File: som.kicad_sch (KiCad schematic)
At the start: 0 parts

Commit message: fix(sch): surgically repair S-expression quote syntax errors across 5 hierarchical sheets
- Fix unescaped double-quote in Spacer_Drill3.7mm_H4mm description on interfaces.kicad_sch line 1459
- Remove backslash-escaped quotes in symbol definitions and lib_id references across display, id-serial, som, and usb-debug sheets (332 lines)
- Restore clean hierarchical schematic loading in KiCad 10 GUI and CLI
- Verified with kicad-cli sch export netlist (full 300 components / 437 nets recovered) and sch erc
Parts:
- added BAT1: Battery_Holder_MS621FE-FL11E, jetson-footprints:MS621FE-FL11E, symbol jetson-symbols:Battery_Holder_MS621FE-FL11E
- added BOOT1, PWR1, USER1: LED_G_0603_LG_L29K-G2J1-24-Z, jetson-footprints:LED_0603_1608Metric_G, symbol jetson-symbols:LED_G_0603_LG_L29K-G2J1-24-Z
- added C10, C11: C_Pol_330u_6.3V_KEMET-T520-B, jetson-footprints:C_Pol_EIA-B, symbol jetson-symbols:C_Pol_330u_6.3V_KEMET-T520-B
- added FB2: FB_10Z_10A_WE-MPSB_1206, jetson-footprints:FB_1206_3216Metric, symbol jetson-symbols:FB_10Z_10A_WE-MPSB_1206
- added J10: Conn_FFC_Molex_5051101097, jetson-footprints:Conn_FFC_Molex_5051101097, symbol jetson-symbols:Conn_FFC_Molex_5051101097
- added J15: Bus_DDR4_SODIMM_CUSTOM_Jetson-Nano-H9.2mm-socket, jetson-footprints:TE_2309413, symbol jetson-symbols:Bus_DDR4_SODIMM_CUSTOM_Jetson-Nano-H9.2mm-socket
- added M2: Jetson-Nano, jetson-footprints:Module_Jetson-Nano, symbol jetson-symbols:Jetson-Nano
- added R111, R14, R97: R_470R_0402, jetson-footprints:R_0402_1005Metric, symbol jetson-symbols:R_470R_0402
- added R112, R113, R139: R_100k_0402, jetson-footprints:R_0402_1005Metric, symbol jetson-symbols:R_100k_0402
- added REC1, RST1, USR1: SW_TL3340AF160QG_SMD, jetson-footprints:SW_TL3340AF160QG_SMD, symbol jetson-symbols:SW_TL3340AF160QG_SMD
- added SP1, SP2, SP3, SP4, SP5, SP6: Spacer_Drill3.7mm_H6mm_9774060151R, jetson-footprints:Spacer_Drill3.7mm_H6mm_9774060151R, symbol jetson-symbols:Spacer_Drill3.7mm_H6mm_9774060151R
- added T2, T4, T5: BSS138PW, jetson-footprints:SC70-3, symbol jetson-symbols:BSS138PW
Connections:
- new net: T5.3 (D), USER1.1 (C)
- new net: R111.2, USER1.2 (A)
- new net: PWR1.1 (C), T4.3 (D)
- new net: PWR1.2 (A), R97.2
- new net: BOOT1.1 (C), T2.3 (D)
- new net: BOOT1.2 (A), R14.2
- new net #PWR_BUTTON: J15.240 (SLEEP/~{WAKE})
- new net #RECOVERY: J15.214 (~{FORCE_RECOVERY}), REC1.2
- new net #RESET: J15.239 (~{SYS_RESET}), R139.1, RST1.2, T2.1 (G)
- new net #SHUTDOWN_REQ: J15.233 (~{SHUTDOWN_REQ})
- new net 1V8_SYS: R112.1
- new net 3V3_SYS: J10.1
- new net 5V0_SYS: FB2.1, R111.1, R14.1, R97.1
- new net CAN_RXD: J15.143 ((CAN_RX)RSVD)
- new net CAN_TXD: J15.145 ((CAN_TX)RSVD)
- new net EGND: SP4.1
- new net ENET_LED0: J15.194 (GBE_LED_ACT)
- new net ENET_LED1: J15.188 (GBE_LED_LINK)
- new net ENET_TRD0_N: J15.184 (GBE_MDI0_N)
- new net ENET_TRD0_P: J15.186 (GBE_MDI0_P)
- new net ENET_TRD1_N: J15.190 (GBE_MDI1_N)
- new net ENET_TRD1_P: J15.192 (GBE_MDI1_P)
- new net ENET_TRD2_N: J15.196 (GBE_MDI2_N)
- new net ENET_TRD2_P: J15.198 (GBE_MDI2_P)
- new net ENET_TRD3_N: J15.202 (GBE_MDI3_N)
- new net ENET_TRD3_P: J15.204 (GBE_MDI3_P)
- new net FAN_PWM: J15.230 (GPIO14)
- new net FAN_TACH: J15.208 (GPIO08)
- new net GEN0_SCL: J15.185 (I2C0_SCL)
- new net GEN0_SDA: J15.187 (I2C0_SDA)
- new net GND: BAT1.2 (-), C10.2, C11.2, J10.10, J15.1 (GND), J15.102 (GND), J15.107 (GND), J15.113 (GND), J15.119 (GND), J15.125 (GND), J15.129 (GND), J15.13 (GND), J15.132 (GND), J15.135 (GND), J15.138 (GND), J15.14 (GND), J15.141 (GND), J15.144 (GND), J15.146 (GND), J15.147 (GND), J15.152 (GND), J15.153 (GND), J15.158 (GND), J15.159 (GND), J15.164 (GND), J15.165 (GND), J15.170 (GND), J15.171 (GND), J15.176 (GND), J15.177 (GND), J15.19 (GND), J15.2 (GND), J15.20 (GND), J15.200 (GND), J15.201 (GND), J15.217 (GND), J15.231 (GND), J15.241 (GND), J15.242 (GND), J15.243 (GND), J15.244 (GND), J15.245 (GND), J15.246 (GND), J15.247 (GND), J15.248 (GND), J15.249 (GND), J15.25 (GND), J15.250 (GND), J15.26 (GND), J15.261 (MNT), J15.262 (MNT), J15.31 (GND), J15.32 (GND), J15.37 (GND), J15.38 (GND), J15.43 (GND), J15.44 (GND), J15.49 (GND), J15.50 (GND), J15.55 (GND), J15.56 (GND), J15.61 (GND), J15.62 (GND), J15.67 (GND), J15.68 (GND), J15.7 (GND), J15.73 (GND), J15.74 (GND), J15.79 (GND), J15.8 (GND), J15.80 (GND), J15.85 (GND), J15.86 (GND), R113.1, R139.2, REC1.1, REC1.3, REC1.SH, RST1.1, RST1.3, RST1.SH, SP1.1, SP2.1, SP3.1, SP5.1, SP6.1, T2.2 (S), T4.2 (S), T5.2 (S), USR1.1, USR1.3, USR1.SH
- new net I2C1_SCL: J15.189 (I2C1_SCL)
- new net I2C1_SDA: J15.191 (I2C1_SDA)
- new net I2C_MUX_RESET: J15.127 (GPIO04)
- new net OTG_USB_D_N: J15.109 (USB0_D_N)
- new net OTG_USB_D_P: J15.111 (USB0_D_P)
- new net PCIE0_CLK_N: J15.160 (PCIE0_CLK_N)
- new net PCIE0_CLK_P: J15.162 (PCIE0_CLK_P)
- new net PCIE0_RX0_N: J15.131 (PCIE0_RX0_N)
- new net PCIE0_RX0_P: J15.133 (PCIE0_RX0_P)
- new net PCIE0_RX1_N: J15.137 (PCIE0_RX1_N)
- new net PCIE0_RX1_P: J15.139 (PCIE0_RX1_P)
- new net PCIE0_RX2_N: J15.149 (PCIE0_RX2_N)
- new net PCIE0_RX2_P: J15.151 (PCIE0_RX2_P)
- new net PCIE0_RX3_N: J15.155 (PCIE0_RX3_N)
- new net PCIE0_RX3_P: J15.157 (PCIE0_RX3_P)
- new net PCIE0_TX0_N: J15.134 (PCIE0_TX0_N)
- new net PCIE0_TX0_P: J15.136 (PCIE0_TX0_P)
- new net PCIE0_TX1_N: J15.140 (PCIE0_TX1_N)
- new net PCIE0_TX1_P: J15.142 (PCIE0_TX1_P)
- new net PCIE0_TX2_N: J15.148 (PCIE0_TX2_N)
- new net PCIE0_TX2_P: J15.150 (PCIE0_TX2_P)
- new net PCIE0_TX3_N: J15.154 (PCIE0_TX3_N)
- new net PCIE0_TX3_P: J15.156 (PCIE0_TX3_P)
- new net PCIE1_CLKREQ: J10.3, J15.182 (PCIE1_CLKREQ)
- new net PCIE1_CLK_N: J10.5, J15.173 (PCIE1_CLK_N)
- new net PCIE1_CLK_P: J10.4, J15.175 (PCIE1_CLK_P)
- new net PCIE1_RST: J10.2, J15.183 (PCIE1_RST)
- new net PCIE1_RX0_N: J10.9, J15.167 (PCIE1_RX0_N)
- new net PCIE1_RX0_P: J10.8, J15.169 (PCIE1_RX0_P)
- new net PCIE1_TX0_N: J10.7, J15.172 (PCIE1_TX0_N)
- new net PCIE1_TX0_P: J10.6, J15.174 (PCIE1_TX0_P)
- new net PEX_L0_CLKREQ_N: J15.180 (~{PCIE0_CLKREQ})
- new net PEX_L0_RST_N: J15.181 (~{PCIE0_RST})
- new net PMIC_BBAT: BAT1.1 (+), J15.235 (PMIC_BBAT)
- new net PWR_EN: J15.237 (POWER_EN)
- new net PWR_GOOD: T4.1 (G)
- new net UART1_RX: J15.238 (UART2_RXD)
- new net UART1_TX: J15.236 (UART2_TXD)
- new net USB1_D_N: J15.115 (USB1_D_N)
- new net USB1_D_P: J15.117 (USB1_D_P)
- new net USBSS_RX6_N: J15.161 (USBSS_RX_N)
- new net USBSS_RX6_P: J15.163 (USBSS_RX_P)
- new net USBSS_TX6_N: J15.166 (USBSS_TX_N)
- new net USBSS_TX6_P: J15.168 (USBSS_TX_P)
- new net USR_BUTTON: R112.2, USR1.2
- new net USR_LED: R113.2, T5.1 (G)
- new net VDD_MOD: C10.1, C11.1, FB2.2, J15.251 (VDD_IN), J15.252 (VDD_IN), J15.253 (VDD_IN), J15.254 (VDD_IN), J15.255 (VDD_IN), J15.256 (VDD_IN), J15.257 (VDD_IN), J15.258 (VDD_IN), J15.259 (VDD_IN), J15.260 (VDD_IN)
- new net VSYNC_CAM1_1: J15.228 (GPIO13)
- new net VSYNC_CAM1_2: J15.216 (GPIO11)
- new net VSYNC_CAM2_2: J15.130 (GPIO06)
- new net \PEWAKE_3V3: J15.179 (~{PCIE_WAKE})
- new net ~{OTG_USB_ID_DET}: J15.128 (GPIO05)
- no-connect marks 0 -> 42
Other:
- note added: "Filtering Capacitors"
- note added: "Mechanical model"
- note added: "Module power"
- note added: "Mounting studs"
- note added: "SoM"
- note added: "System Buttons"
- note added: "System Status"
- note added: "Text"
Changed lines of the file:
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@@
 	)
 	(symbol
-		(lib_id \"jetson-symbols:LED_G_0603_LG_L29K-G2J1-24-Z\")
+		(lib_id "jetson-symbols:LED_G_0603_LG_L29K-G2J1-24-Z")
 		(at 370.84 118.11 270)
 		(mirror x)
@@
 	)
 	(symbol
-		(lib_id \"jetson-symbols:Bus_DDR4_SODIMM_CUSTOM_Jetson-Nano-H9.2mm-socket\")
+		(lib_id "jetson-symbols:Bus_DDR4_SODIMM_CUSTOM_Jetson-Nano-H9.2mm-socket")
 		(at 68.58 177.8 0)
 		(unit 7)
@@
 	)
 	(symbol
-		(lib_id \"jetson-symbols:Bus_DDR4_SODIMM_CUSTOM_Jetson-Nano-H9.2mm-socket\")
+		(lib_id "jetson-symbols:Bus_DDR4_SODIMM_CUSTOM_Jetson-Nano-H9.2mm-socket")
 		(at 207.01 146.05 0)
 		(unit 6)
@@
 	)
 	(symbol
-		(lib_id \"jetson-symbols:Bus_DDR4_SODIMM_CUSTOM_Jetson-Nano-H9.2mm-socket\")
+		(lib_id "jetson-symbols:Bus_DDR4_SODIMM_CUSTOM_Jetson-Nano-H9.2mm-socket")
 		(at 69.85 125.73 0)
 		(unit 4)
@@
 	)
 	(symbol
-		(lib_id \"jetson-symbols:Bus_DDR4_SODIMM_CUSTOM_Jetson-Nano-H9.2mm-socket\")
+		(lib_id "jetson-symbols:Bus_DDR4_SODIMM_CUSTOM_Jetson-Nano-H9.2mm-socket")
 		(at 41.91 45.72 0)
 		(unit 1)
@@
 	)
 	(symbol
-		(lib_id \"jetson-symbols:Bus_DDR4_SODIMM_CUSTOM_Jetson-Nano-H9.2mm-socket\")
+		(lib_id "jetson-symbols:Bus_DDR4_SODIMM_CUSTOM_Jetson-Nano-H9.2mm-socket")
 		(at 207.01 35.56 0)
 		(unit 3)
@@
 	)
 	(symbol
-		(lib_id \"jetson-symbols:BSS138PW\")
+		(lib_id "jetson-symbols:BSS138PW")
 		(at 302.26 132.08 0)
 		(mirror y)
@@
 	)
 	(symbol
-		(lib_id \"jetson-symbols:BSS138PW\")
+		(lib_id "jetson-symbols:BSS138PW")
 		(at 339.09 132.08 0)
 		(mirror y)
@@
 	)
 	(symbol
-		(lib_id \"jetson-symbols:BSS138PW\")
+		(lib_id "jetson-symbols:BSS138PW")
 		(at 378.46 132.08 0)
 		(mirror y)
@@
 	)
 	(symbol
-		(lib_id \"jetson-symbols:SW_TL3340AF160QG_SMD\")
+		(lib_id "jetson-symbols:SW_TL3340AF160QG_SMD")
 		(at 297.18 199.39 0)
 		(unit 1)
@@
 	)
 	(symbol
-		(lib_id \"jetson-symbols:Conn_FFC_Molex_5051101097\")
+		(lib_id "jetson-symbols:Conn_FFC_Molex_5051101097")
 		(at 290.83 33.02 0)
 		(unit 1)
@@
 	)
 	(symbol
-		(lib_id \"jetson-symbols:Spacer_Drill3.7mm_H6mm_9774060151R\")
+		(lib_id "jetson-symbols:Spacer_Drill3.7mm_H6mm_9774060151R")
 		(at 379.73 238.76 0)
 		(unit 1)
@@
 	)
 	(symbol
-		(lib_id \"jetson-symbols:Spacer_Drill3.7mm_H6mm_9774060151R\")
+		(lib_id "jetson-symbols:Spacer_Drill3.7mm_H6mm_9774060151R")
 		(at 379.73 226.06 0)
 		(unit 1)
@@
 	)
 	(symbol
-		(lib_id \"jetson-symbols:Battery_Holder_MS621FE-FL11E\")
+		(lib_id "jetson-symbols:Battery_Holder_MS621FE-FL11E")
 		(at 350.52 73.66 0)
 		(unit 1)
@@
 	)
 	(symbol
-		(lib_id \"jetson-symbols:Spacer_Drill3.7mm_H6mm_9774060151R\")
+		(lib_id "jetson-symbols:Spacer_Drill3.7mm_H6mm_9774060151R")
 		(at 350.52 238.76 0)
 		(unit 1)
@@
 	)
 	(symbol
-		(lib_id \"jetson-symbols:Spacer_Drill3.7mm_H6mm_9774060151R\")
+		(lib_id "jetson-symbols:Spacer_Drill3.7mm_H6mm_9774060151R")
 		(at 350.52 226.06 0)
 		(unit 1)
@@
 	)
 	(symbol
-		(lib_id \"jetson-symbols:Jetson-Nano\")
+		(lib_id "jetson-symbols:Jetson-Nano")
 		(at 255.905 260.35 0)
 		(unit 1)
@@
 	)
 	(symbol
-		(lib_id \"jetson-symbols:Spacer_Drill3.7mm_H6mm_9774060151R\")
+		(lib_id "jetson-symbols:Spacer_Drill3.7mm_H6mm_9774060151R")
 		(at 321.31 238.76 0)
 		(unit 1)
@@
 	)
 	(symbol
-		(lib_id \"jetson-symbols:LED_G_0603_LG_L29K-G2J1-24-Z\")
+		(lib_id "jetson-symbols:LED_G_0603_LG_L29K-G2J1-24-Z")
 		(at 331.47 118.11 270)
 		(mirror x)
@@
 	)
 	(symbol
-		(lib_id \"jetson-symbols:LED_G_0603_LG_L29K-G2J1-24-Z\")
+		(lib_id "jetson-symbols:LED_G_0603_LG_L29K-G2J1-24-Z")
 		(at 294.64 118.11 270)
 		(mirror x)
@@
 	)
 	(symbol
-		(lib_id \"jetson-symbols:Spacer_Drill3.7mm_H6mm_9774060151R\")
+		(lib_id "jetson-symbols:Spacer_Drill3.7mm_H6mm_9774060151R")
 		(at 321.31 226.06 0)
 		(unit 1)
@@
 	)
 	(symbol
-		(lib_id \"jetson-symbols:C_Pol_330u_6.3V_KEMET-T520-B\")
+		(lib_id "jetson-symbols:C_Pol_330u_6.3V_KEMET-T520-B")
 		(at 364.49 35.56 270)
 		(unit 1)
@@
 	)
 	(symbol
-		(lib_id \"jetson-symbols:C_Pol_330u_6.3V_KEMET-T520-B\")
+		(lib_id "jetson-symbols:C_Pol_330u_6.3V_KEMET-T520-B")
 		(at 350.52 35.56 270)
 		(unit 1)
@@
 	)
 	(symbol
-		(lib_id \"jetson-symbols:R_100k_0402\")
+		(lib_id "jetson-symbols:R_100k_0402")
 		(at 314.96 191.77 270)
 		(unit 1)
@@
 	)
 	(symbol
-		(lib_id \"jetson-symbols:R_470R_0402\")
+		(lib_id "jetson-symbols:R_470R_0402")
 		(at 294.64 105.41 270)
 		(unit 1)
@@
 	)
 	(symbol
-		(lib_id \"jetson-symbols:R_470R_0402\")
+		(lib_id "jetson-symbols:R_470R_0402")
 		(at 331.47 105.41 270)
 		(unit 1)
@@
 	)
 	(symbol
-		(lib_id \"jetson-symbols:R_470R_0402\")
+		(lib_id "jetson-symbols:R_470R_0402")
 		(at 370.84 105.41 270)
 		(unit 1)
@@
 	)
 	(symbol
-		(lib_id \"jetson-symbols:SW_TL3340AF160QG_SMD\")
+		(lib_id "jetson-symbols:SW_TL3340AF160QG_SMD")
 		(at 297.18 168.91 0)
 		(unit 1)
@@
 	)
 	(symbol
-		(lib_id \"jetson-symbols:R_100k_0402\")
+		(lib_id "jetson-symbols:R_100k_0402")
 		(at 379.73 137.16 0)
 		(unit 1)
@@
 	)
 	(symbol
-		(lib_id \"jetson-symbols:SW_TL3340AF160QG_SMD\")
+		(lib_id "jetson-symbols:SW_TL3340AF160QG_SMD")
 		(at 297.18 184.15 0)
 		(unit 1)
@@
 	)
 	(symbol
-		(lib_id \"jetson-symbols:R_100k_0402\")
+		(lib_id "jetson-symbols:R_100k_0402")
 		(at 115.57 57.15 270)
 		(unit 1)
@@
 	)
 	(symbol
-		(lib_id \"jetson-symbols:FB_10Z_10A_WE-MPSB_1206\")
+		(lib_id "jetson-symbols:FB_10Z_10A_WE-MPSB_1206")
 		(at 364.49 62.23 0)
 		(unit 1)
@@
 	)
 	(symbol
-		(lib_id \"jetson-symbols:GND\")
+		(lib_id "jetson-symbols:GND")
 		(at 287.02 57.15 0)
 		(unit 1)
@@
 	)
 	(symbol
-		(lib_id \"jetson-symbols:GND\")
+		(lib_id "jetson-symbols:GND")
 		(at 350.52 85.09 0)
 		(unit 1)
@@
 	)
 	(symbol
-		(lib_id \"jetson-symbols:GND\")
+		(lib_id "jetson-symbols:GND")
 		(at 370.84 138.43 0)
 		(unit 1)
@@
 	)
 	(symbol
-		(lib_id \"jetson-symbols:GND\")
+		(lib_id "jetson-symbols:GND")
 		(at 317.5 228.6 0)
 		(unit 1)
@@
 	)
 	(symbol
-		(lib_id \"jetson-symbols:GND\")
+		(lib_id "jetson-symbols:GND")
 		(at 331.47 138.43 0)
 		(unit 1)
@@
 	)
 	(symbol
-		(lib_id \"jetson-symbols:GND\")
+		(lib_id "jetson-symbols:GND")
 		(at 294.64 138.43 0)
 		(unit 1)
@@
 	)
 	(symbol
-		(lib_id \"jetson-symbols:GND\")
+		(lib_id "jetson-symbols:GND")
 		(at 289.56 209.55 0)
 		(unit 1)
@@
 	)
 	(symbol
-		(lib_id \"jetson-symbols:GND\")
+		(lib_id "jetson-symbols:GND")
 		(at 349.25 241.3 0)
 		(unit 1)
@@
 	)
 	(symbol
-		(lib_id \"jetson-symbols:GND\")
+		(lib_id "jetson-symbols:GND")
 		(at 378.46 241.3 0)
 		(unit 1)
@@
 	)
 	(symbol
-		(lib_id \"jetson-symbols:GND\")
+		(lib_id "jetson-symbols:GND")
 		(at 364.49 43.18 0)
 		(unit 1)
@@
 	)
 	(symbol
-		(lib_id \"jetson-symbols:GND\")
+		(lib_id "jetson-symbols:GND")
 		(at 350.52 43.18 0)
 		(unit 1)
@@
 	)
 	(symbol
-		(lib_id \"jetson-symbols:GND\")
+		(lib_id "jetson-symbols:GND")
 		(at 39.37 68.58 0)
 		(unit 1)
@@
 	)
 	(symbol
-		(lib_id \"jetson-symbols:GND\")
+		(lib_id "jetson-symbols:GND")
 		(at 115.57 64.77 0)
 		(unit 1)

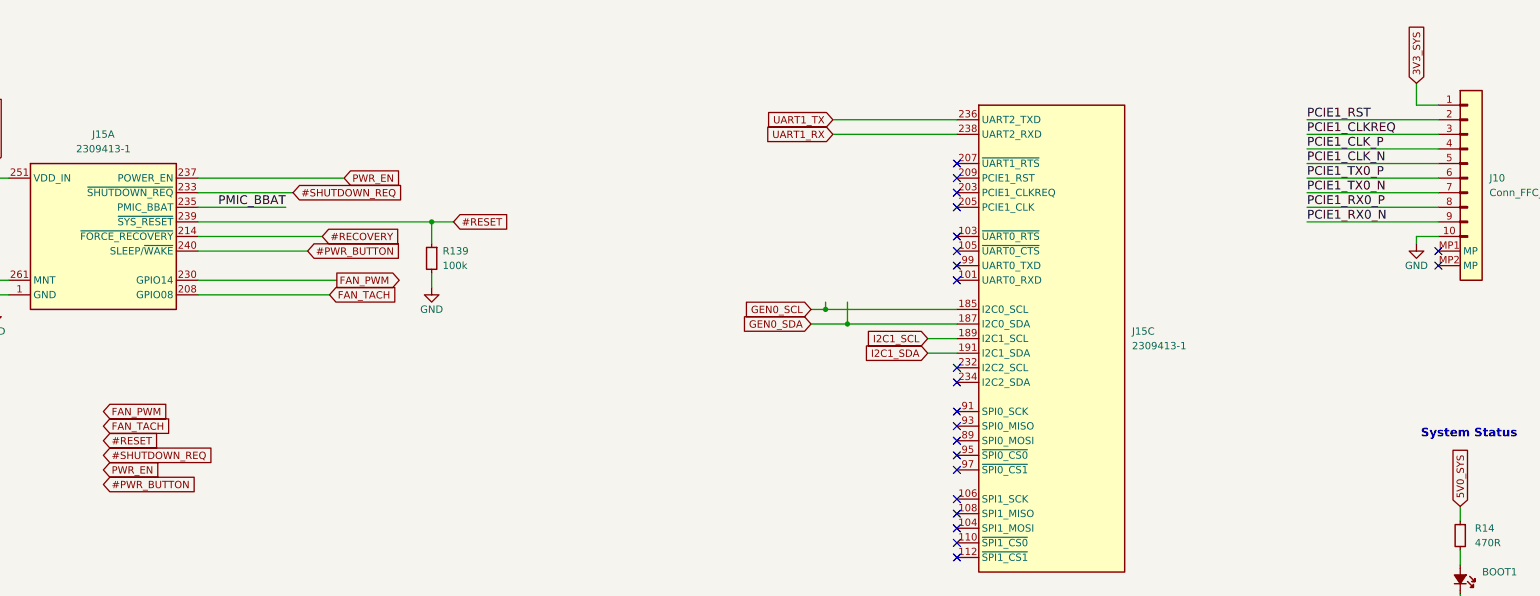
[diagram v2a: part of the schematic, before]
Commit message: fix(schematic): remediate camera clocking, power sequencing, and ERC errors
- Connect Sony IMX219 master clocks (CAM0/1_MCLK) from SoM pins 116/122
- Connect independent PWDN hardware resets from SoM pins 114/120
- Isolate sensor I2C channels (CAM0/1_SCL/SDA) downstream of PCA9547
- Upgrade U11 digital core LDO to TLV75512PDBVR (500mA rating)
- Ground R132 to enable serial EEPROM write-protect
- Connect 3V3_SYS power rail to CAN transceiver U7 and fuse F5
- Eliminate dangling global labels across all sheets
- Configure 25 mil connection grid and achieve 0 ERC errors
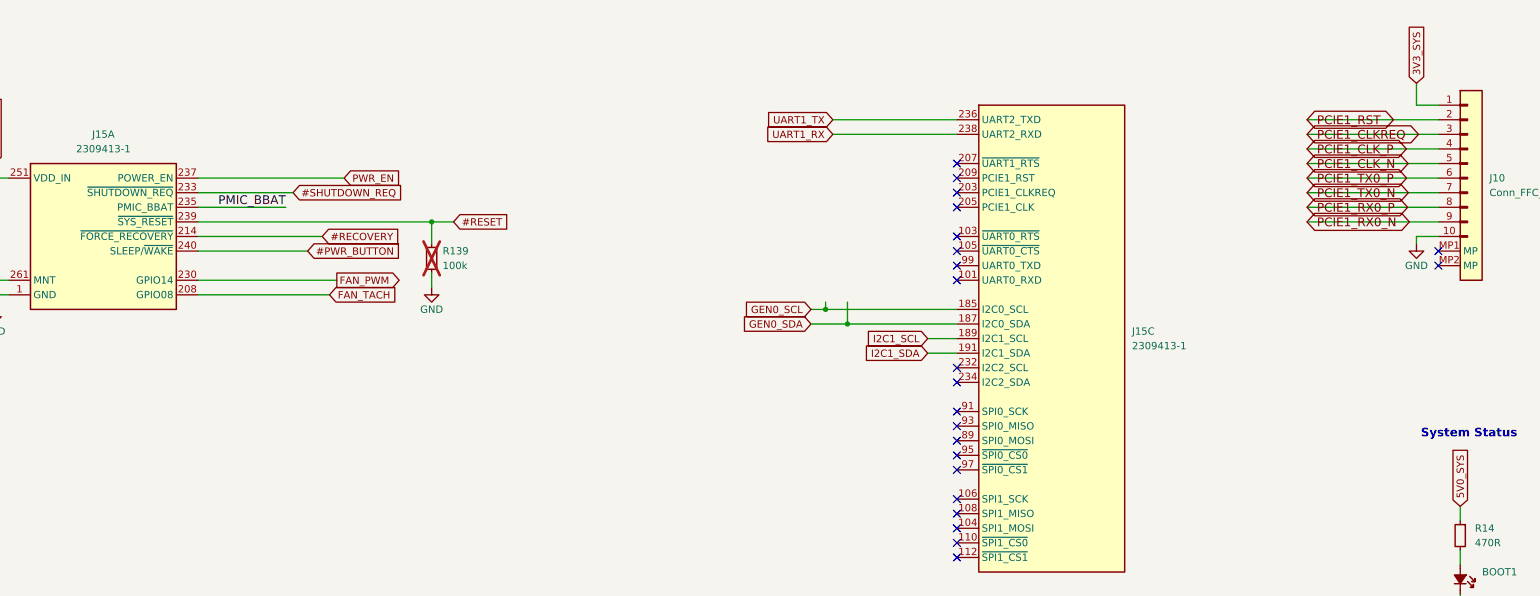
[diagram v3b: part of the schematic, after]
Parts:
- R139: now not fitted
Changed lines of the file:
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@@
 		(on_board yes)
 		(in_pos_files yes)
-		(dnp no)
+		(dnp yes)
 		(fields_autoplaced yes)
 		(property "Reference" "R139"
@@
 		)
 	)
-	(label "PCIE1_TX0_N"
+	(global_label "PCIE1_TX0_N"
+		(shape bidirectional)
 		(at 267.97 48.26 0)
 		(effects
@@
 		)
 	)
-	(label "PCIE1_CLKREQ"
+	(global_label "PCIE1_CLKREQ"
+		(shape bidirectional)
 		(at 267.97 38.1 0)
 		(effects
@@
 		)
 	)
-	(label "PCIE1_CLK_N"
+	(global_label "PCIE1_CLK_N"
+		(shape bidirectional)
 		(at 267.97 43.18 0)
 		(effects
@@
 		)
 	)
-	(label "PCIE1_RX0_P"
+	(global_label "PCIE1_RX0_P"
+		(shape bidirectional)
 		(at 267.97 50.8 0)
 		(effects
@@
 		)
 	)
-	(label "PCIE1_RST"
+	(global_label "PCIE1_RST"
+		(shape bidirectional)
 		(at 267.97 35.56 0)
 		(effects
@@
 		)
 	)
-	(label "PCIE1_RX0_N"
+	(global_label "PCIE1_RX0_N"
+		(shape bidirectional)
 		(at 267.97 53.34 0)
 		(effects
@@
 		)
 	)
-	(label "PCIE1_CLK_P"
+	(global_label "PCIE1_CLK_P"
+		(shape bidirectional)
 		(at 267.97 40.64 0)
 		(effects
@@
 		)
 	)
-	(label "PCIE1_TX0_P"
+	(global_label "PCIE1_TX0_P"
+		(shape bidirectional)
 		(at 267.97 45.72 0)
 		(effects
@@
 		)
 	)
-	(global_label "PWR_EN"
-		(shape input)
-		(at 58.42 96.52 0)
-		(fields_autoplaced yes)
-		(effects
-			(font
-				(size 1.27 1.27)
-			)
-			(justify left)
-		)
-		(property "Intersheetrefs" "${INTERSHEET_REFS}"
-			(at -59.055 13.335 0)
-			(hide yes)
-			(show_name no)
-			(do_not_autoplace no)
-			(effects
-				(font
-					(size 1.27 1.27)
-				)
-			)
-		)
-	)
 	(global_label "PCIE1_TX0_N"
 		(shape input)
@@
 		)
 	)
-	(global_label "FAN_PWM"
-		(shape input)
-		(at 58.42 86.36 0)
-		(fields_autoplaced yes)
-		(effects
-			(font
-				(size 1.27 1.27)
-			)
-			(justify left)
-		)
-		(property "Intersheetrefs" "${INTERSHEET_REFS}"
-			(at -59.055 13.335 0)
-			(hide yes)
-			(show_name no)
-			(do_not_autoplace no)
-			(effects
-				(font
-					(size 1.27 1.27)
-				)
-			)
-		)
-	)
 	(global_label "PCIE0_RX3_P"
 		(shape input)
@@
 		)
 	)
-	(global_label "#SHUTDOWN_REQ"
-		(shape input)
-		(at 58.42 93.98 0)
-		(fields_autoplaced yes)
-		(effects
-			(font
-				(size 1.27 1.27)
-			)
-			(justify left)
-		)
-		(property "Intersheetrefs" "${INTERSHEET_REFS}"
-			(at -59.055 13.335 0)
-			(hide yes)
-			(show_name no)
-			(do_not_autoplace no)
-			(effects
-				(font
-					(size 1.27 1.27)
-				)
-			)
-		)
-	)
 	(global_label "PCIE0_TX1_P"
 		(shape input)
@@
 		)
 	)
-	(global_label "FAN_TACH"
-		(shape input)
-		(at 58.42 88.9 0)
-		(fields_autoplaced yes)
-		(effects
-			(font
-				(size 1.27 1.27)
-			)
-			(justify left)
-		)
-		(property "Intersheetrefs" "${INTERSHEET_REFS}"
-			(at -59.055 13.335 0)
-			(hide yes)
-			(show_name no)
-			(do_not_autoplace no)
-			(effects
-				(font
-					(size 1.27 1.27)
-				)
-			)
-		)
-	)
 	(global_label "ENET_TRD0_P"
 		(shape input)
@@
 			(hide yes)
 			(show_name no)
-			(do_not_autoplace no)
-			(effects
-				(font
-					(size 1.27 1.27)
-				)
-			)
-		)
-	)
-	(global_label "#PWR_BUTTON"
-		(shape input)
-		(at 58.42 99.06 0)
-		(fields_autoplaced yes)
-		(effects
-			(font
-				(size 1.27 1.27)
-			)
-			(justify left)
-		)
-		(property "Intersheetrefs" "${INTERSHEET_REFS}"
-			(at -59.055 13.335 0)
-			(hide yes)
-			(show_name no)
-			(do_not_autoplace no)
-			(effects
-				(font
-					(size 1.27 1.27)
-				)
-			)
-		)
-	)
-	(global_label "#RESET"
-		(shape input)
-		(at 58.42 91.44 0)
-		(fields_autoplaced yes)
-		(effects
-			(font
-				(size 1.27 1.27)
-			)
-			(justify left)
-		)
-		(property "Intersheetrefs" "${INTERSHEET_REFS}"
-			(at -59.055 13.335 0)
-			(hide yes)
-			(show_name no)
